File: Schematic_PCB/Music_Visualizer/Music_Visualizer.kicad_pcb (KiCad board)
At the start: 2 copper layers, 141.4 x 82 mm, 273 parts, among them J1 NMJ4HCD2, J2 Barrel_Jack_PTH, J3 Screw_Terminal_01x02, J4 NMJ4HCD2, J5 Screw_Terminal_01x02, J6 3.5mm, Q1 DMP2123LQ-7, SW1 SW_Slide_DPDT, SW2 SW_SPST, U1 LM324, U10 LM3915N-1, U11 LM3915N-1, U12 LM3915N-1, U13 LM3915N-1, U14 LM3915N-1, U15 LM3915N-1, U16 LM3915N-1, U2 LM324, U3 LM324, U4 LM324, U5 LM324, U6 LM324, U7 LM324, U8 LM324

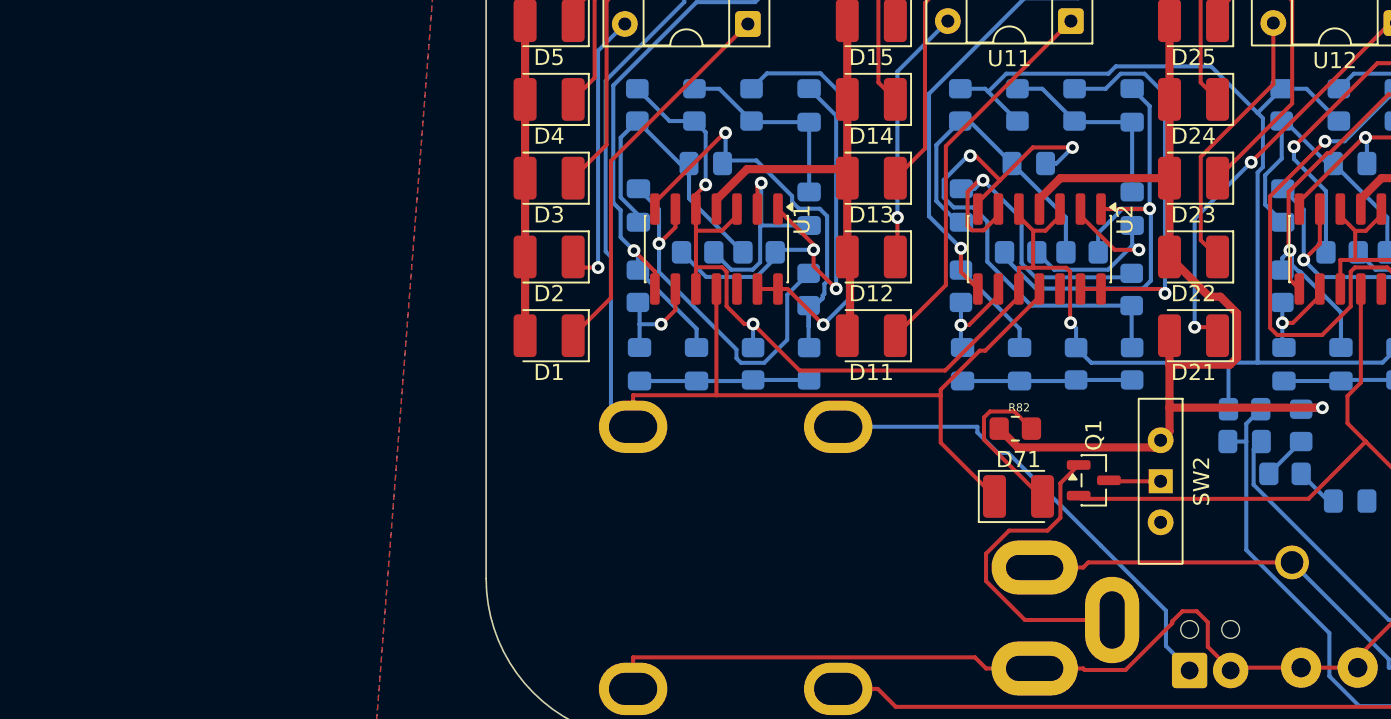
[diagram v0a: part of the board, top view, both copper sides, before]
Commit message: Change Barrel jack footprint
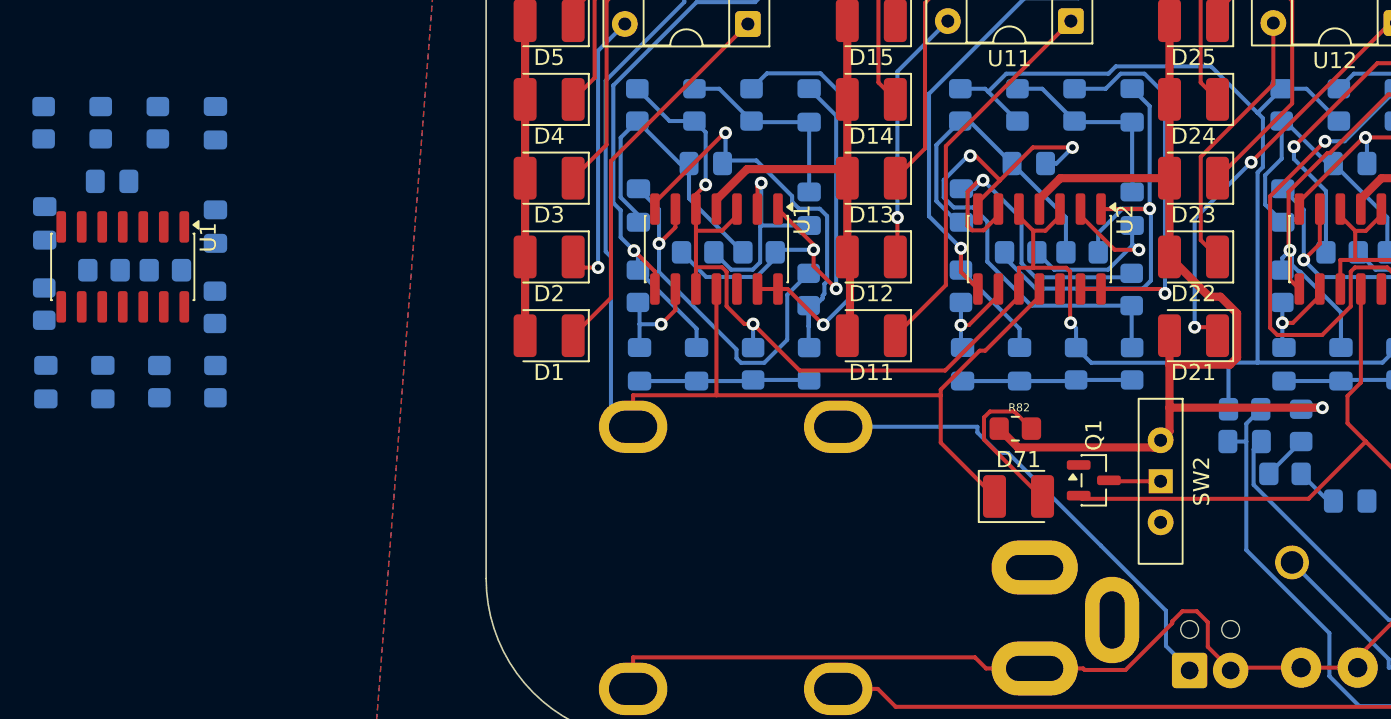
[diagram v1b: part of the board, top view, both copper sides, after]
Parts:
- added C1: 220n, Custom_Footprints:C_0805_2012Metric_Pad1.18x1.45mm_HandSolder, B.Cu at (-4.66, 55.8)
- added C2: 220n, Custom_Footprints:C_0805_2012Metric_Pad1.18x1.45mm_HandSolder, B.Cu at (-4.66, 62.2)
- added C3: 220n, Custom_Footprints:C_0805_2012Metric_Pad1.18x1.45mm_HandSolder, B.Cu at (-11.1, 59.4)
- added C4: 220n, Custom_Footprints:C_0805_2012Metric_Pad1.18x1.45mm_HandSolder, B.Cu at (-15.2, 62.0)
- added C5: 220n, Custom_Footprints:C_0805_2012Metric_Pad1.18x1.45mm_HandSolder, B.Cu at (-11.6, 71.8)
- added C6: 220n, Custom_Footprints:C_0805_2012Metric_Pad1.18x1.45mm_HandSolder, B.Cu at (-15.2, 71.8)
- added R1: 27k, Custom_Footprints:R_0805_2012Metric_Pad1.20x1.40mm_HandSolder, B.Cu at (-8.23, 55.8)
- added R2: 12k, Custom_Footprints:R_0805_2012Metric_Pad1.20x1.40mm_HandSolder, B.Cu at (-11.8, 55.8)
- added R3: 150k, Custom_Footprints:R_0805_2012Metric_Pad1.20x1.40mm_HandSolder, B.Cu at (-11.6, 64.9)
- added R4: 10k, Custom_Footprints:R_0805_2012Metric_Pad1.20x1.40mm_HandSolder, B.Cu at (-7.76, 64.9)
- added R5: 4.7k, Custom_Footprints:R_0805_2012Metric_Pad1.20x1.40mm_HandSolder, B.Cu at (-15.3, 55.8)
- added R6: 47k, Custom_Footprints:R_0805_2012Metric_Pad1.20x1.40mm_HandSolder, B.Cu at (-4.69, 67.2)
- added R7: 18k, Custom_Footprints:R_0805_2012Metric_Pad1.20x1.40mm_HandSolder, B.Cu at (-4.66, 71.8)
- added R8: 39k, Custom_Footprints:R_0805_2012Metric_Pad1.20x1.40mm_HandSolder, B.Cu at (-8.13, 71.8)
- added R9: 39k, Custom_Footprints:R_0805_2012Metric_Pad1.20x1.40mm_HandSolder, B.Cu at (-15.3, 67.0)
- added U1: LM324, Package_SO:SOIC-14_3.9x8.7mm_P1.27mm, F.Cu at (-10.4, 64.7)
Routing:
- net Net-(J2-GND): track 19.8 -> 0.00 mm
- net Net-(J2-GNDBREAK): track 26.6 -> 10.6 mm

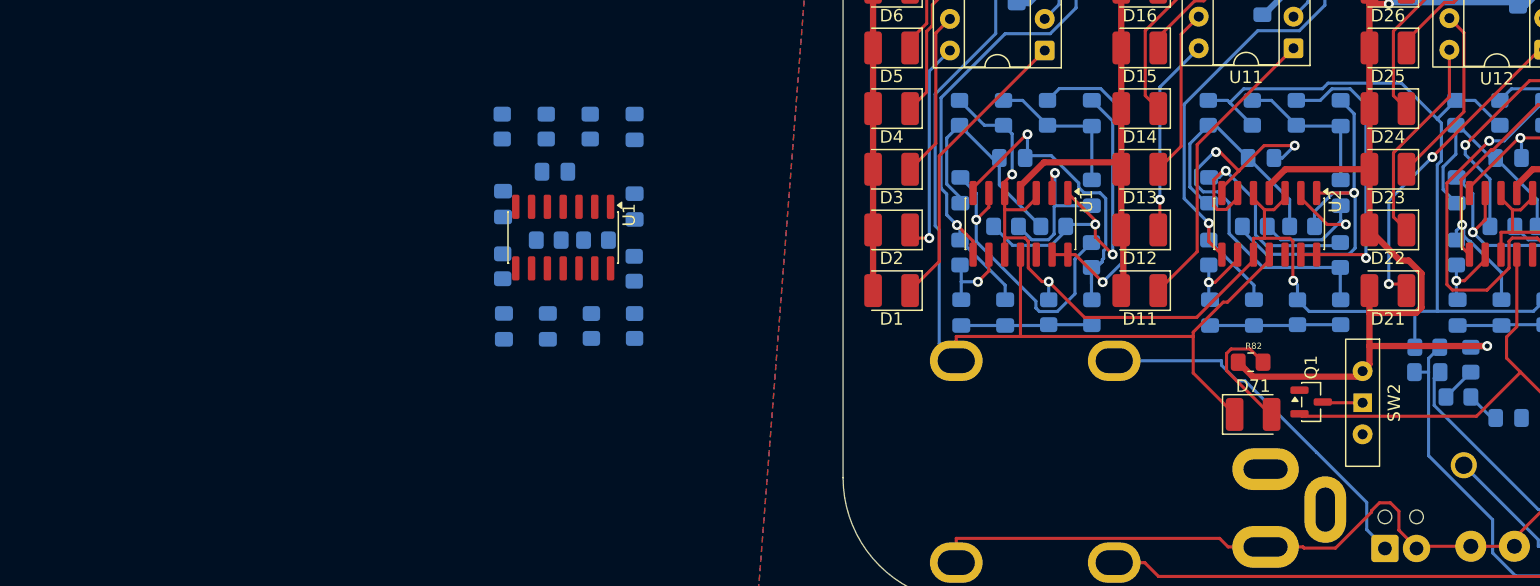
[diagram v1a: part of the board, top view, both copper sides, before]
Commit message: Update capacitor footprint
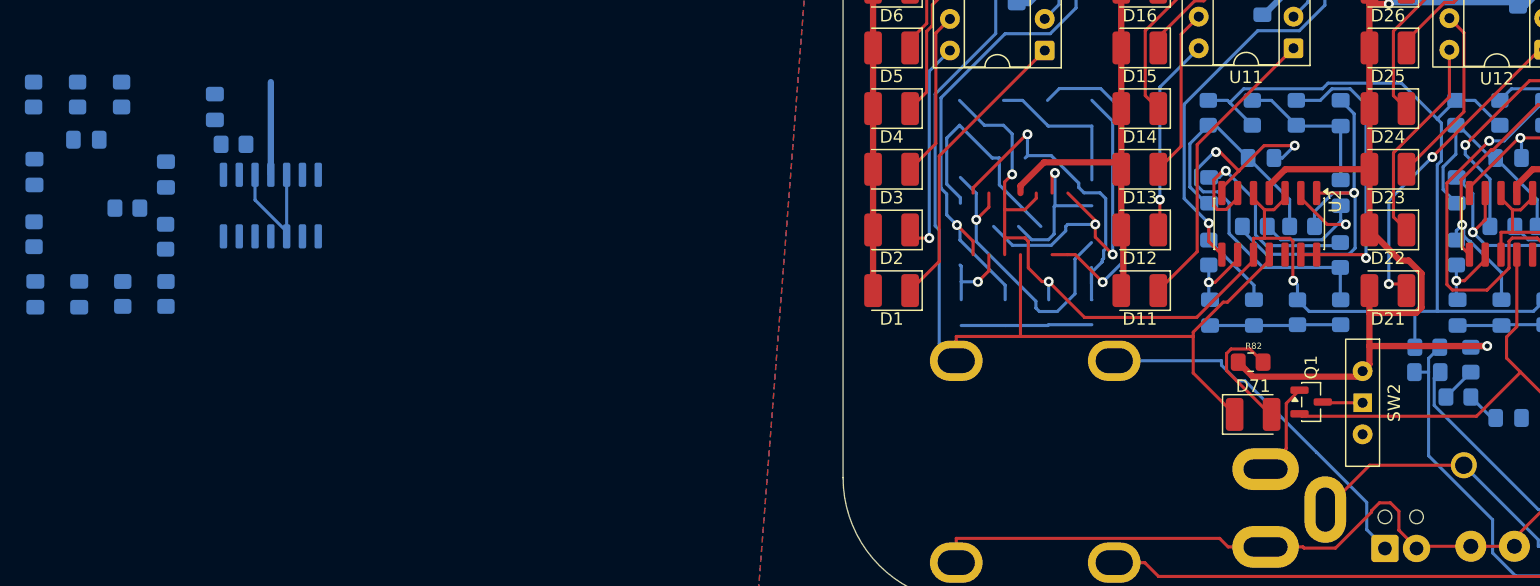
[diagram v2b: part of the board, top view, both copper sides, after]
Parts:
- removed the C1 at (-4.66, 55.8)
- removed the C2 at (-4.66, 62.2)
- removed the C3 at (-11.1, 59.4)
- removed the C4 at (-15.2, 62.0)
- removed the C5 at (-11.6, 71.8)
- removed the C6 at (-15.2, 71.8)
- removed the R1 at (-8.23, 55.8)
- removed the R2 at (-11.8, 55.8)
- removed the R3 at (-11.6, 64.9)
- removed the R4 at (-7.76, 64.9)
- removed the R5 at (-15.3, 55.8)
- removed the R6 at (-4.69, 67.2)
- removed the R7 at (-4.66, 71.8)
- removed the R8 at (-8.13, 71.8)
- removed the R9 at (-15.3, 67.0)
- removed the U1 at (-10.4, 64.7)
- C1, C11, C12, C13, C14, C15, C16, C18, C19, C2, C20, C21, C22, C23, C25, C26, C27, C28, C29, C3, C30, C31, C32, C33, C34, C35, C36, C37, C38, C39, C4, C40, C41, C42, C44, C45, C46, C47, C48, C49, C5, C50, C51, C52, C53, C55, C56, C59, C6, C60, C61, C62, C63, C64, C65, C66, C67, C68, C69, C7, C70, C71, C72, C73, C74, C9: footprint Custom_Footprints:C_0805_2012Metric_Pad1.18x1.45mm_HandSolder -> Custom_Footprints:custom_C_0805_2012Metric_Pad1.18x1.45mm_HandSolder
- U1: moved to B.Cu
- moved C2 74.4 mm to (-42.3, 59.6)
- moved C3 74.4 mm to (-48.7, 56.8)
- moved C4 74.4 mm to (-52.9, 59.4)
- moved C5 74.4 mm to (-49.3, 69.3)
- moved C6 74.4 mm to (-52.8, 69.3)
- moved R1 74.4 mm to (-45.9, 53.2)
- moved R2 74.4 mm to (-49.4, 53.2)
- moved R4 74.4 mm to (-45.4, 62.3)
- moved R5 74.4 mm to (-53.0, 53.2)
- moved R6 74.4 mm to (-42.4, 64.6)
- moved R7 74.4 mm to (-42.3, 69.2)
- moved R8 74.4 mm to (-45.8, 69.2)
- moved R9 74.4 mm to (-52.9, 64.4)
- moved C1 70.5 mm to (-38.4, 54.2), turned to -90 degrees
- moved R3 62.4 mm to (-36.9, 57.2)
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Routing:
- net Net-(J2-GNDBREAK): track 10.6 -> 23.2 mm
- net VCC4_5: track 374.1 -> 385.1 mm
- net Net-(J2-GND): track 0.00 -> 7.48 mm
- net +9V: track 763.4 -> 770.9 mm

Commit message: Test layout
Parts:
- removed the C1 at (-38.4, 54.2)
- removed the C2 at (-42.3, 59.6)
- removed the C3 at (-48.7, 56.8)
- removed the C4 at (-52.9, 59.4)
- removed the C5 at (-49.3, 69.3)
- removed the C59 at (86.7, 81.5)
- removed the C6 at (-52.8, 69.3)
- removed C67, C68, C69, C70, C71, C72, C73, C74: 100n, Custom_Footprints:custom_C_0805_2012Metric_Pad1.18x1.45mm_HandSolder
- removed D71: LED, LED_SMD:LED_1210_3225Metric_Pad1.42x2.65mm_HandSolder
- removed the R1 at (-45.9, 53.2)
- removed the R2 at (-49.4, 53.2)
- removed the R3 at (-36.9, 57.2)
- removed the R4 at (-45.4, 62.3)
- removed the R5 at (-53.0, 53.2)
- removed the R6 at (-42.4, 64.6)
- removed the R7 at (-42.3, 69.2)
- removed the R8 at (-45.8, 69.2)
- removed the R9 at (-52.9, 64.4)
- removed the U1 at (-33.9, 62.1)
- added C1: 220n, Custom_Footprints:custom_C_0805_2012Metric_Pad1.18x1.45mm_HandSolder, B.Cu at (-113.6, 55.0)
- added C1: 220n, Custom_Footprints:custom_C_0805_2012Metric_Pad1.18x1.45mm_HandSolder, B.Cu at (-63.2, 50.4)
- added C2: 220n, Custom_Footprints:custom_C_0805_2012Metric_Pad1.18x1.45mm_HandSolder, B.Cu at (-113.7, 53.0)
- added C2: 220n, Custom_Footprints:custom_C_0805_2012Metric_Pad1.18x1.45mm_HandSolder, B.Cu at (-60.4, 50.4)
- added C3: 220n, Custom_Footprints:custom_C_0805_2012Metric_Pad1.18x1.45mm_HandSolder, B.Cu at (-53.8, 50.4)
- added C3: 220n, Custom_Footprints:custom_C_0805_2012Metric_Pad1.18x1.45mm_HandSolder, B.Cu at (-114.4, 47.5)
- added C4: 220n, Custom_Footprints:custom_C_0805_2012Metric_Pad1.18x1.45mm_HandSolder, B.Cu at (-56.4, 50.4)
- added C4: 220n, Custom_Footprints:custom_C_0805_2012Metric_Pad1.18x1.45mm_HandSolder, B.Cu at (-114.4, 49.5)
- added C43: 10u, Custom_Footprints:custom_C_0805_2012Metric_Pad1.18x1.45mm_HandSolder, F.Cu at (-122.9, 46.7)
- added C43: 10u, Custom_Footprints:custom_C_0805_2012Metric_Pad1.18x1.45mm_HandSolder, B.Cu at (-53.6, 64.4)
- added C5: 220n, Custom_Footprints:custom_C_0805_2012Metric_Pad1.18x1.45mm_HandSolder, B.Cu at (-58.6, 65.0)
- added C5: 220n, Custom_Footprints:custom_C_0805_2012Metric_Pad1.18x1.45mm_HandSolder, B.Cu at (-122.2, 47.7)
- added C59: 100n, Custom_Footprints:custom_C_0805_2012Metric_Pad1.18x1.45mm_HandSolder, B.Cu at (-118.4, 53.7)
- added C59: 100n, Custom_Footprints:custom_C_0805_2012Metric_Pad1.18x1.45mm_HandSolder, B.Cu at (-58.4, 52.5)
- added C6: 220n, Custom_Footprints:custom_C_0805_2012Metric_Pad1.18x1.45mm_HandSolder, B.Cu at (-122.2, 49.7)
- added C6: 220n, Custom_Footprints:custom_C_0805_2012Metric_Pad1.18x1.45mm_HandSolder, B.Cu at (-62.4, 63.7)
- added D1: LED, PCM_SparkFun-LED:LED_1206_3216Metric_Green, F.Cu at (-118.4, 43.7)
- added D10: LED, PCM_SparkFun-LED:LED_1206_3216Metric_Green, F.Cu at (-118.4, 23.4)
- added D2: LED, PCM_SparkFun-LED:LED_1206_3216Metric_Green, F.Cu at (-118.4, 41.4)
- added D3: LED, PCM_SparkFun-LED:LED_1206_3216Metric_Green, F.Cu at (-118.4, 39.2)
- added D4: LED, PCM_SparkFun-LED:LED_1206_3216Metric_Green, F.Cu at (-118.4, 36.9)
- added D5: LED, PCM_SparkFun-LED:LED_1206_3216Metric_Green, F.Cu at (-118.4, 34.7)
- added D6: LED, PCM_SparkFun-LED:LED_1206_3216Metric_Green, F.Cu at (-118.4, 32.4)
- added D7: LED, PCM_SparkFun-LED:LED_1206_3216Metric_Green, F.Cu at (-118.4, 30.2)
- added D8: LED, PCM_SparkFun-LED:LED_1206_3216Metric_Green, F.Cu at (-118.4, 27.9)
- added D9: LED, PCM_SparkFun-LED:LED_1206_3216Metric_Green, F.Cu at (-118.4, 25.7)
- added H3: MountingHole, MountingHole:MountingHole_3.2mm_M3, F.Cu at (-13.2, 88.0)
- added H4: MountingHole, MountingHole:MountingHole_3.2mm_M3, F.Cu at (-13.2, 96.0)
- added R1: 27k, Custom_Footprints:R_0805_2012Metric_Pad1.20x1.40mm_HandSolder, F.Cu at (-113.1, 54.0)
- added R1: 27k, Custom_Footprints:R_0805_2012Metric_Pad1.20x1.40mm_HandSolder, B.Cu at (-64.4, 57.7)
- added R2: 12k, Custom_Footprints:R_0805_2012Metric_Pad1.20x1.40mm_HandSolder, F.Cu at (-118.6, 45.7)
- added R2: 12k, Custom_Footprints:R_0805_2012Metric_Pad1.20x1.40mm_HandSolder, B.Cu at (-60.4, 46.5)
- added R3: 150k, Custom_Footprints:R_0805_2012Metric_Pad1.20x1.40mm_HandSolder, B.Cu at (-61.4, 53.2)
- added R3: 150k, Custom_Footprints:R_0805_2012Metric_Pad1.20x1.40mm_HandSolder, B.Cu at (-116.4, 53.7)
- added R4: 10k, Custom_Footprints:R_0805_2012Metric_Pad1.20x1.40mm_HandSolder, F.Cu at (-112.9, 49.2)
- added R4: 10k, Custom_Footprints:R_0805_2012Metric_Pad1.20x1.40mm_HandSolder, B.Cu at (-58.4, 48.0)
- added R5: 4.7k, Custom_Footprints:R_0805_2012Metric_Pad1.20x1.40mm_HandSolder, F.Cu at (-114.1, 45.7)
- added R5: 4.7k, Custom_Footprints:R_0805_2012Metric_Pad1.20x1.40mm_HandSolder, B.Cu at (-58.4, 43.5)
- added R6: 47k, Custom_Footprints:R_0805_2012Metric_Pad1.20x1.40mm_HandSolder, B.Cu at (-55.4, 53.2)
- added R6: 47k, Custom_Footprints:R_0805_2012Metric_Pad1.20x1.40mm_HandSolder, B.Cu at (-117.2, 48.5)
- added R66: 1k, Custom_Footprints:R_0805_2012Metric_Pad1.20x1.40mm_HandSolder, B.Cu at (-57.9, 36.0)
- added R66: 1k, Custom_Footprints:R_0805_2012Metric_Pad1.20x1.40mm_HandSolder, B.Cu at (-116.7, 31.9)
- added R7: 18k, Custom_Footprints:R_0805_2012Metric_Pad1.20x1.40mm_HandSolder, B.Cu at (-55.6, 64.5)
- added R7: 18k, Custom_Footprints:R_0805_2012Metric_Pad1.20x1.40mm_HandSolder, B.Cu at (-119.9, 45.7)
- added R75: 680, Custom_Footprints:R_0805_2012Metric_Pad1.20x1.40mm_HandSolder, B.Cu at (-116.4, 27.2)
- added R75: 680, Custom_Footprints:R_0805_2012Metric_Pad1.20x1.40mm_HandSolder, B.Cu at (-57.6, 27.4)
- added R8: 39k, Custom_Footprints:R_0805_2012Metric_Pad1.20x1.40mm_HandSolder, B.Cu at (-122.1, 51.7)
- added R8: 39k, Custom_Footprints:R_0805_2012Metric_Pad1.20x1.40mm_HandSolder, B.Cu at (-64.4, 61.7)
- added R9: 39k, Custom_Footprints:R_0805_2012Metric_Pad1.20x1.40mm_HandSolder, B.Cu at (-119.2, 48.5)
- added R9: 39k, Custom_Footprints:R_0805_2012Metric_Pad1.20x1.40mm_HandSolder, B.Cu at (-58.6, 63.0)
- added TP1: T_SB, Custom_Footprints:TEST1Y, B.Cu at (-58.6, 22.4)
- added TP1: T_SB, Custom_Footprints:TEST1Y, B.Cu at (-117.4, 18.4)
- added U1: LM324, Package_SO:SOIC-14_3.9x8.7mm_P1.27mm, F.Cu at (-118.1, 51.2)
- added U1: LM324, Package_SO:SOIC-14_3.9x8.7mm_P1.27mm, B.Cu at (-58.8, 58.0)
- added U10: LM3915N-1, Package_DIP:DIP-18_W7.62mm_Socket, F.Cu at (-55.1, 47.2)
- added U10: LM3915N-1, Package_DIP:DIP-18_W7.62mm_Socket, B.Cu at (-122.2, 43.5)
- C43: footprint Capacitor_SMD:CP_Elec_4x5.4 -> Custom_Footprints:custom_C_0805_2012Metric_Pad1.18x1.45mm_HandSolder
- C60, C61, C62, C63, C64, C65, C66: moved to F.Cu
- D1, D10, D11, D12, D13, D14, D15, D16, D17, D18, D19, D2, D20, D21, D22, D23, D24, D25, D26, D27, D28, D29, D3, D30, D31, D32, D33, D34, D35, D36, D37, D38, D39, D4, D40, D41, D42, D43, D44, D45, D46, D47, D48, D49, D5, D50, D51, D52, D53, D54, D55, D56, D57, D58, D59, D6, D60, D61, D62, D63, D64, D65, D66, D67, D68, D69, D7, D70, D8, D9: footprint LED_SMD:LED_1210_3225Metric_Pad1.42x2.65mm_HandSolder -> PCM_SparkFun-LED:LED_1206_3216Metric_Green
- moved C66 124.1 mm to (-21.5, 106.6), turned to 0 degrees
- moved C65 107.7 mm to (-21.5, 103.6), turned to 0 degrees
- moved C64 103.9 mm to (-21.5, 100.6), turned to 0 degrees
- moved C63 87.5 mm to (-21.5, 97.6), turned to 0 degrees
- moved C62 83.2 mm to (-21.5, 94.6), turned to 0 degrees
- moved C61 69.6 mm to (-21.5, 91.5), turned to 0 degrees
- moved C60 64.6 mm to (-21.5, 88.5), turned to 0 degrees
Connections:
- C61 pad 2: GND -> +9V
- C63 pad 2: GND -> +9V
- C65 pad 2: GND -> +9V
- TP10 pad 1: Net-(J2-GNDBREAK) -> Net-(J2-GND)
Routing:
- net VSubBass: track 18.8 -> 49.2 mm
- net Net-(C3-Pad2): track 26.4 -> 39.7 mm
- net Net-(U1D--): track 26.6 -> 39.7 mm
- net Net-(C1-Pad2): track 29.2 -> 40.1 mm
- net Net-(C43-Pad1): track 39.8 -> 49.2 mm
- net Net-(C3-Pad1): track 18.3 -> 26.7 mm
- net Net-(C5-Pad1): track 10.5 -> 18.3 mm
- net Net-(C1-Pad1): track 12.3 -> 19.4 mm
- net Net-(U1C--): track 6.72 -> 11.6 mm
- net Net-(U1B--): track 24.1 -> 28.3 mm
- net VCC4_5: track 385.1 -> 388.9 mm, vias 11 -> 13
- net Net-(U1A--): track 13.1 -> 15.1 mm
- net +9V: track 770.9 -> 772.6 mm, vias 11 -> 12
- net Vsig: vias 0 -> 1

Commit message: Remove jacks and compact placement
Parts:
- removed the C1 at (-63.2, 50.4)
- removed the C2 at (-60.4, 50.4)
- removed the C3 at (-53.8, 50.4)
- removed the C4 at (-56.4, 50.4)
- removed the C43 at (-53.6, 64.4)
- removed the C43 at (30.8, 40.5)
- removed the C5 at (-58.6, 65.0)
- removed the C59 at (-58.4, 52.5)
- removed the C6 at (-62.4, 63.7)
- removed the D1 at (16.0, 69.0)
- removed the D10 at (16.0, 25.1)
- removed the D2 at (16.0, 64.1)
- removed the D3 at (16.0, 59.2)
- removed the D4 at (16.0, 54.3)
- removed the D5 at (16.0, 49.5)
- removed the D6 at (16.0, 44.6)
- removed the D7 at (16.0, 39.7)
- removed the D8 at (16.0, 34.8)
- removed the D9 at (16.0, 29.9)
- removed J1, J4: NMJ4HCD2, Custom_Footprints:Jack_6.35mm
- removed J2: Barrel_Jack_PTH, Custom_Footprints:RAPC722X
- removed the R1 at (-64.4, 57.7)
- removed the R2 at (-60.4, 46.5)
- removed the R3 at (-61.4, 53.2)
- removed the R4 at (-58.4, 48.0)
- removed the R5 at (-58.4, 43.5)
- removed the R6 at (-55.4, 53.2)
- removed the R66 at (30.8, 36.7)
- removed the R66 at (-57.9, 36.0)
- removed the R7 at (-55.6, 64.5)
- removed the R75 at (-57.6, 27.4)
- removed the R75 at (25.8, 33.3)
- removed the R8 at (-64.4, 61.7)
- removed the R9 at (-58.6, 63.0)
- removed the TP1 at (29.5, 24.7)
- removed the TP1 at (-58.6, 22.4)
- removed the TP1 at (-117.4, 18.4)
- removed the U1 at (-58.8, 58.0)
- removed the U10 at (28.3, 49.7)
- removed the U10 at (-55.1, 47.2)
- added D71: LED, PCM_SparkFun-LED:LED_1206_3216Metric_Red, F.Cu at (44.8, 76.8)
- added TP1: T_SB, Custom_Footprints:TEST1Y, F.Cu at (18.5, 16.9)
- C17, C24: footprint Capacitor_SMD:CP_Elec_4x5.4 -> Custom_Footprints:custom_C_0805_2012Metric_Pad1.18x1.45mm_HandSolder; moved to F.Cu
- C31, C38, C46, C53, R13, R14, R16, R17, R23, R24, R26, R27, R33, R34, R36, R37, R43, R44, R46, R47, R53, R54, R56, R57, R63, R64, R67, R68, TP2, TP3, TP4, TP5, TP6, TP7: moved to F.Cu
- C60, C61, C62, C63, C64, C65, C66: moved to B.Cu
- D10, D20, D30, D40, D50, D60, D70: footprint PCM_SparkFun-LED:LED_1206_3216Metric_Green -> PCM_SparkFun-LED:LED_1206_3216Metric_Red
- D18, D19, D28, D29, D38, D39, D48, D49, D58, D59, D68, D69, D8, D9: footprint PCM_SparkFun-LED:LED_1206_3216Metric_Green -> PCM_SparkFun-LED:LED_1206_3216Metric_Yellow
- H1: footprint MountingHole:MountingHole_3.2mm_M3 -> MountingHole:MountingHole_3.2mm_M3_DIN965
- U10: footprint Package_DIP:DIP-18_W7.62mm_Socket -> Package_DIP:DIP-18_W7.62mm
- U11, U12, U13, U14, U15, U16: footprint Package_DIP:DIP-18_W7.62mm_Socket -> Package_DIP:DIP-18_W7.62mm; moved to B.Cu
- moved H3 190.6 mm to (165.7, 22.1)
- moved H4 190.6 mm to (165.7, 30.1)
- moved R5 138.0 mm to (23.8, 47.3), turned to -90 degrees
- moved R2 137.3 mm to (18.6, 43.1)
- moved C6 137.0 mm to (14.8, 48.1)
- moved D1 137.0 mm to (18.6, 40.9)
- moved D2 137.0 mm to (18.6, 38.6)
- moved D4 137.0 mm to (18.6, 34.1)
- moved U10 137.0 mm to (14.8, 40.7)
- moved D10 137.0 mm to (18.6, 20.6)
- moved D3 137.0 mm to (18.6, 36.3)
- moved D5 137.0 mm to (18.6, 31.8)
- moved D6 137.0 mm to (18.6, 29.6)
- moved D7 137.0 mm to (18.6, 27.3)
- moved D8 137.0 mm to (18.6, 25.1)
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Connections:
- C43 pad 1: Net-(C43-Pad1) -> VSubBass
- C43 pad 2: VSubBass -> Net-(C43-Pad2)
- C5 pad 2: Net-(C43-Pad1) -> Net-(C43-Pad2)
- J3 pad 1: Net-(J3-Pin_1) -> Left jack
- J5 pad 1: Net-(J5-Pin_1) -> Right jack
- J6 pad 1: Net-(J2-GNDBREAK) -> Net-(J6-Pin_1)
- Q1 pad 1: Net-(J2-GND) -> Net-(J6-Pin_1)
- R12 pad 1: Net-(C8-Pad1) -> Net-(C8-Pad2)
- R85 pad 2: Net-(C8-Pad2) -> Net-(C8-Pad1)
- R9 pad 1: Net-(C43-Pad1) -> Net-(C43-Pad2)
- SW1 pad 5: Net-(C8-Pad1) -> Net-(C8-Pad2)
- TP10 pad 1: Net-(J2-GND) -> Net-(J6-Pin_1)
- TP14 pad 1: Net-(C8-Pad1) -> Net-(C8-Pad2)
- U1 pad 8: Net-(C43-Pad1) -> Net-(C43-Pad2)
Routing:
- net GND: track 555.2 -> 0.00 mm, vias 2 -> 0
- net +9V: track 772.6 -> 432.7 mm, vias 12 -> 9
- net Mode: track 217.2 -> 0.00 mm
- net Vsig: track 0.00 -> 159.6 mm, vias 1 -> 0
- net LED_Brightness_Control: track 236.4 -> 353.9 mm, vias 2 -> 0
- net VCC4_5: track 388.9 -> 321.0 mm, vias 13 -> 8
- net Net-(U8A-+): track 60.3 -> 0.00 mm
- net Left jack: track 53.5 -> 0.00 mm
- net Net-(C43-Pad1): track 49.2 -> 0.00 mm, vias 1 -> 0
- net Rhi_Value: track 189.7 -> 237.4 mm, vias 2 -> 0
- net Net-(C29-Pad2): track 46.5 -> 4.48 mm
- net Net-(C36-Pad2): track 43.8 -> 4.48 mm
- net Net-(C34-Pad2): track 39.9 -> 2.44 mm, vias 4 -> 0
- net Net-(C3-Pad2): track 39.7 -> 2.44 mm, vias 1 -> 0
- net Net-(C15-Pad2): track 40.3 -> 4.48 mm
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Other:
- board size 141.4 x 82 mm -> 141.5 x 82 mm
- board text added: "Bass[60Hz:150Hz]"
- board text added: "Brilliance[6kHz:20kHz]"
- board text added: "Low Midrange[150Hz:400Hz]"
- board text added: "Midrange[400Hz:1kHz]"
- board text added: "Presence[2.5kHz:6kHz]"
- board text added: "Upper-Midrange[1kHz:2.5kHz]"
- board text removed: "11"
- board text removed: "12"
- board text removed: "Bass [60Hz:150Hz]"
- board text removed: "Brilliance [6kHz:20kHz]"
- board text removed: "Low Midrange [150Hz:400Hz]"
- board text removed: "Midrange [400Hz:1kHz]"
- board text removed: "Presence [2.5kHz:6kHz]"
- board text removed: "Upper-Midrange [1kHz:2.5kHz]"
